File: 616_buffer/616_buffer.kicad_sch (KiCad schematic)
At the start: 25 parts, among them J1 1K_Zero, J2 Edge_J104, J3 Air_Pin, U1 LM317L_SO8, U2 LM337L_SO8, U3 LMC6081

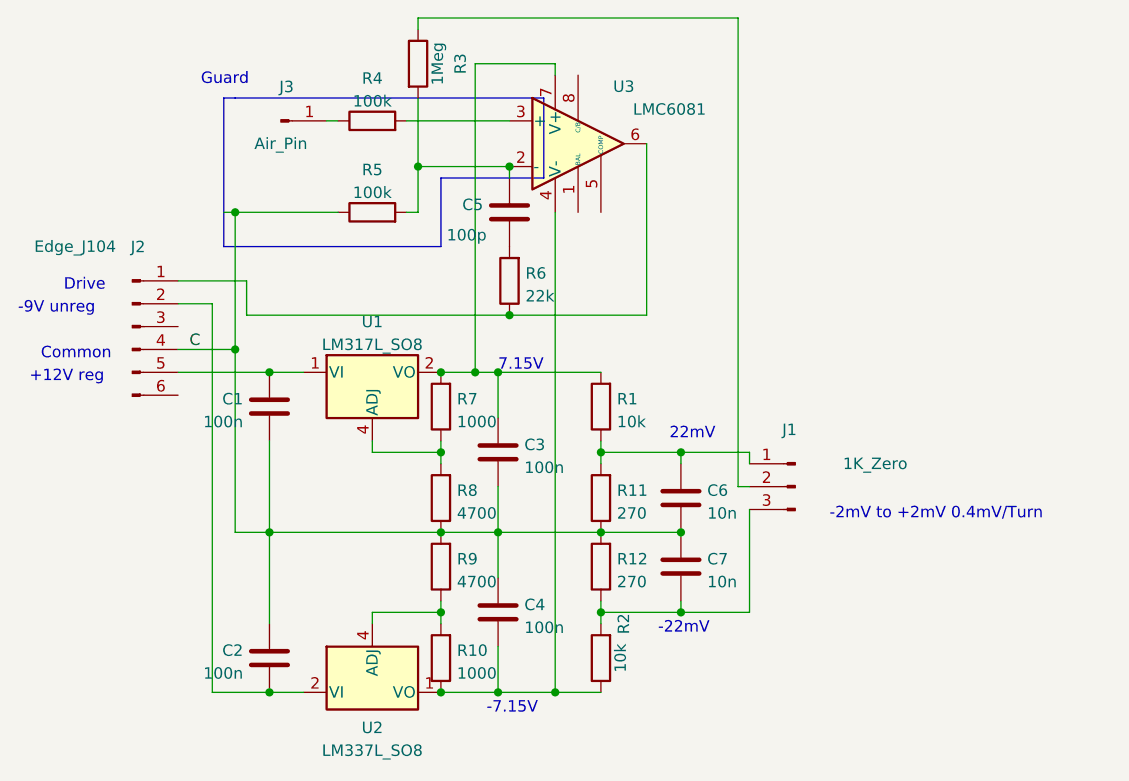
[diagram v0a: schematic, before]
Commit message: Fixed zero connector pinout
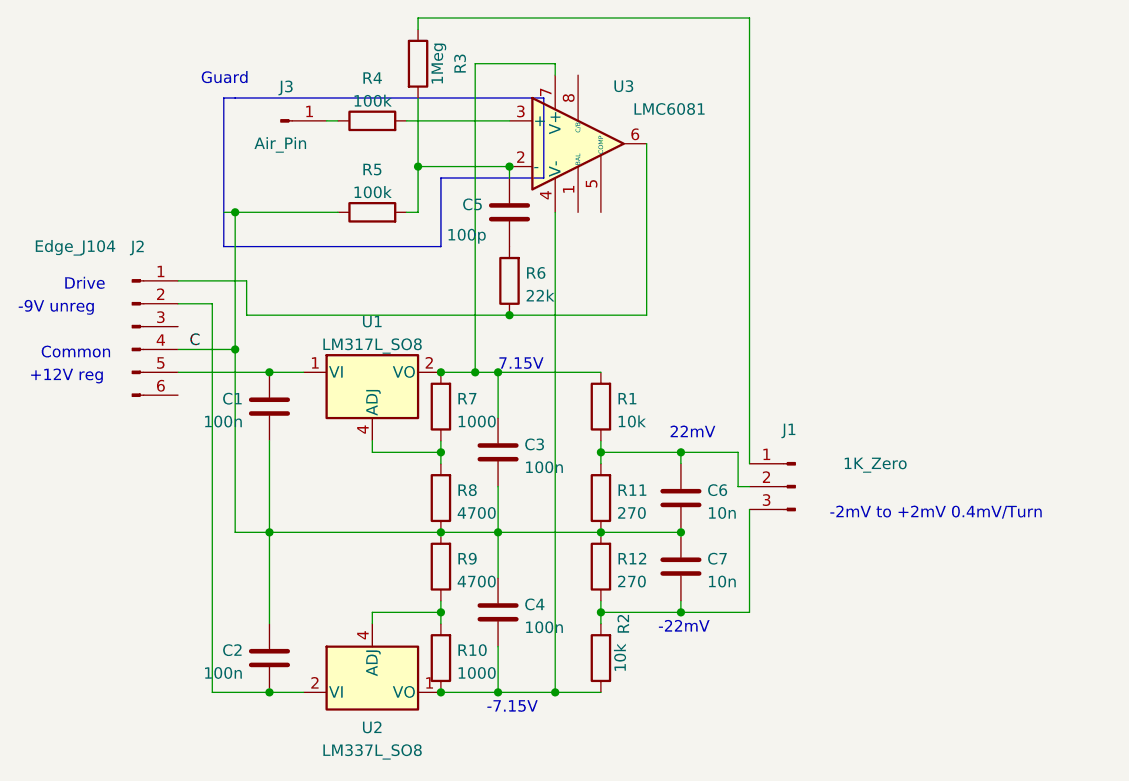
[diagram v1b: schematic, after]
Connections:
- net at C6.2, R1.1, R11.2: now also J1.2 (Pin_2); no longer J1.1 (Pin_1)
- net at R3.1: now also J1.1 (Pin_1); no longer J1.2 (Pin_2)
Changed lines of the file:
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@@
   (junction (at 99.06 102.87) (diameter 0) (color 0 0 0 0)
   )
+  (junction (at 114.3 161.29) (diameter 0) (color 0 0 0 0)
+  )
+  (junction (at 82.55 143.51) (diameter 0) (color 0 0 0 0)
+  )
+  (junction (at 107.95 125.73) (diameter 0) (color 0 0 0 0)
+  )
+  (junction (at 105.41 125.73) (diameter 0) (color 0 0 0 0)
+  )
+  (junction (at 109.22 119.38) (diameter 0) (color 0 0 0 0)
+  )
+  (junction (at 101.6 152.4) (diameter 0) (color 0 0 0 0)
+  )
+  (junction (at 107.95 161.29) (diameter 0) (color 0 0 0 0)
+  )
+  (junction (at 119.38 143.51) (diameter 0) (color 0 0 0 0)
+  )
+  (junction (at 101.6 134.62) (diameter 0) (color 0 0 0 0)
+  )
+  (junction (at 78.74 107.95) (diameter 0) (color 0 0 0 0)
+  )
+  (junction (at 101.6 125.73) (diameter 0) (color 0 0 0 0)
+  )
   (junction (at 128.27 134.62) (diameter 0) (color 0 0 0 0)
   )
-  (junction (at 114.3 161.29) (diameter 0) (color 0 0 0 0)
-  )
-  (junction (at 82.55 143.51) (diameter 0) (color 0 0 0 0)
-  )
-  (junction (at 107.95 125.73) (diameter 0) (color 0 0 0 0)
-  )
-  (junction (at 105.41 125.73) (diameter 0) (color 0 0 0 0)
-  )
-  (junction (at 109.22 119.38) (diameter 0) (color 0 0 0 0)
-  )
-  (junction (at 101.6 152.4) (diameter 0) (color 0 0 0 0)
-  )
-  (junction (at 107.95 161.29) (diameter 0) (color 0 0 0 0)
-  )
-  (junction (at 119.38 143.51) (diameter 0) (color 0 0 0 0)
-  )
-  (junction (at 101.6 134.62) (diameter 0) (color 0 0 0 0)
-  )
-  (junction (at 78.74 107.95) (diameter 0) (color 0 0 0 0)
-  )
-  (junction (at 101.6 125.73) (diameter 0) (color 0 0 0 0)
-  )
   (junction (at 101.6 161.29) (diameter 0) (color 0 0 0 0)
   )
@@
   (junction (at 128.27 152.4) (diameter 0) (color 0 0 0 0)
   )
-  (wire (pts (xy 134.62 86.36) (xy 99.06 86.36))
-    (stroke (width 0) (type default) (color 0 0 0 0))
-  )
-  (wire (pts (xy 135.89 134.62) (xy 128.27 134.62))
+  (wire (pts (xy 99.06 86.36) (xy 135.89 86.36))
     (stroke (width 0) (type default) (color 0 0 0 0))
   )
@@
     (stroke (width 0) (type default) (color 0 0 0 0))
   )
+  (wire (pts (xy 135.89 138.43) (xy 134.62 138.43))
+    (stroke (width 0) (type default) (color 0 0 0 0))
+  )
   (wire (pts (xy 119.38 161.29) (xy 114.3 161.29))
     (stroke (width 0) (type default) (color 0 0 0 0))
@@
     (stroke (width 0) (type default) (color 0 0 0 0))
   )
+  (wire (pts (xy 135.89 135.89) (xy 135.89 86.36))
+    (stroke (width 0) (type default) (color 0 0 0 0))
+  )
   (wire (pts (xy 101.6 161.29) (xy 107.95 161.29))
     (stroke (width 0) (type default) (color 0 0 0 0))
@@
     (stroke (width 0) (type default) (color 0 0 0 0))
   )
-  (wire (pts (xy 135.89 138.43) (xy 134.62 138.43))
-    (stroke (width 0) (type default) (color 0 0 0 0))
-  )
   (polyline (pts (xy 78.74 111.76) (xy 101.6 111.76))
     (stroke (width 0) (type default) (color 0 0 0 0))
@@
     (stroke (width 0) (type default) (color 0 0 0 0))
   )
-  (wire (pts (xy 134.62 138.43) (xy 134.62 86.36))
-    (stroke (width 0) (type default) (color 0 0 0 0))
-  )
   (polyline (pts (xy 77.47 95.25) (xy 78.74 95.25))
     (stroke (width 0) (type default) (color 0 0 0 0))
@@
     (stroke (width 0) (type default) (color 0 0 0 0))
   )
-  (wire (pts (xy 135.89 135.89) (xy 135.89 134.62))
-    (stroke (width 0) (type default) (color 0 0 0 0))
-  )
   (wire (pts (xy 88.9 97.79) (xy 90.17 97.79))
     (stroke (width 0) (type default) (color 0 0 0 0))
   )
+  (wire (pts (xy 128.27 134.62) (xy 134.62 134.62))
+    (stroke (width 0) (type default) (color 0 0 0 0))
+  )
   (wire (pts (xy 105.41 125.73) (xy 107.95 125.73))
     (stroke (width 0) (type default) (color 0 0 0 0))
@@
     (stroke (width 0) (type default) (color 0 0 0 0))
   )
+  (wire (pts (xy 134.62 138.43) (xy 134.62 134.62))
+    (stroke (width 0) (type default) (color 0 0 0 0))
+  )
